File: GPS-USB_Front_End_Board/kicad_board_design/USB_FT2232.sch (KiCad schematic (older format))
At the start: 38 parts, among them J1 Micro-USB Connector, U1 93LCxxB, U2 FT2232HL-REEL, U3 L4931 LDO, Y1 12MHz Crystal

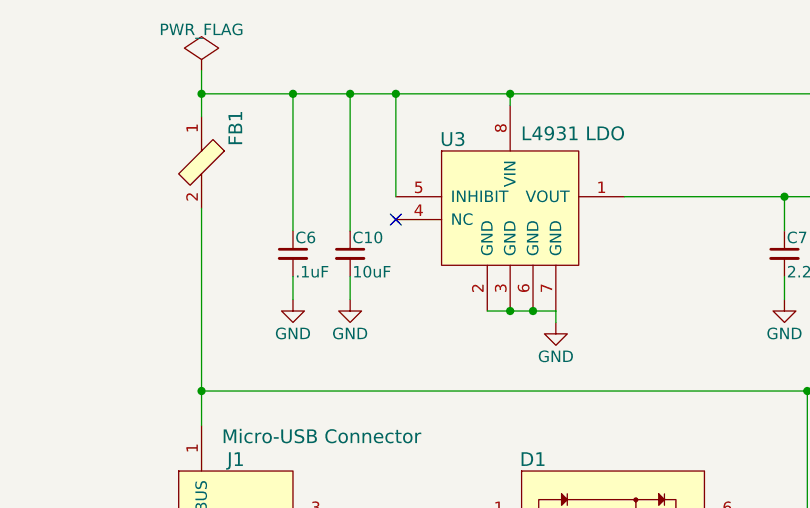
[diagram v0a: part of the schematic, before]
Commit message: Fix 3.3V LDO inhibit polarity.
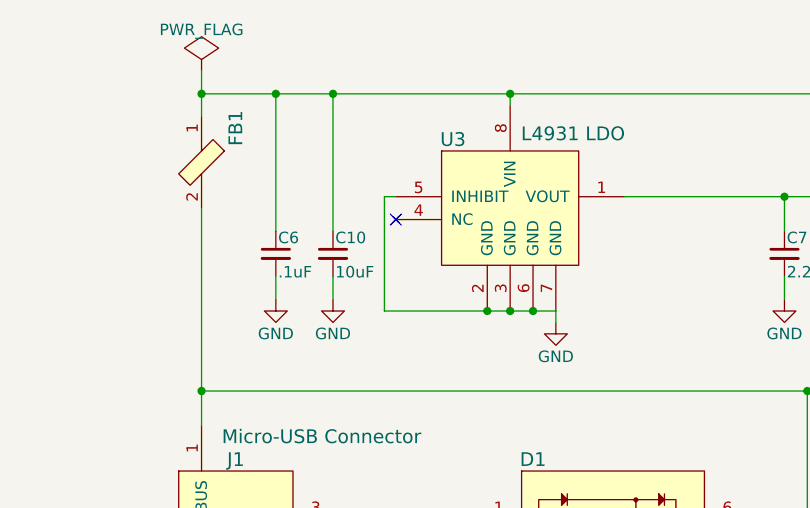
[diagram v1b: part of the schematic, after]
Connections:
- net +5V: no longer U3.5 (INHIBIT)
- net GND: now also U3.5 (INHIBIT)
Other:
- moved on the sheet: C10, C6

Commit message: Change out micro-usb connector to one with thru holes.
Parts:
- J1: footprint digikey-footprints:USB_Micro_B_Female_10118192 -> digikey-footprints:USB_Micro_B_Female_10118194-0001LF; Digi-Key_PN 609-4613-1-ND -> 609-4618-6-ND; MPN 10118192-0001LF -> 10118194-0001LF
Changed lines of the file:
@@
 F 0 "J1" H 7450 3000 60  0000 C CNN
 F 1 "Micro-USB Connector" H 7825 3100 60  0000 C CNN
-F 2 "digikey-footprints:USB_Micro_B_Female_10118192" H 7600 2950 60  0001 L CNN
+F 2 "digikey-footprints:USB_Micro_B_Female_10118194-0001LF" H 7600 2950 60  0001 L CNN
 F 3 "https://cdn.amphenol-icc.com/media/wysiwyg/files/drawing/10118192.pdf" H 7600 3050 60  0001 L CNN
-F 4 "609-4613-1-ND" H 7600 3150 60  0001 L CNN "Digi-Key_PN"
-F 5 "10118192-0001LF" H 7600 3250 60  0001 L CNN "MPN"
+F 4 "609-4618-6-ND" H 7600 3150 60  0001 L CNN "Digi-Key_PN"
+F 5 "10118194-0001LF" H 7600 3250 60  0001 L CNN "MPN"
 F 6 "Connectors, Interconnects" H 7600 3350 60  0001 L CNN "Category"
 F 7 "USB, DVI, HDMI Connectors" H 7600 3450 60  0001 L CNN "Family"

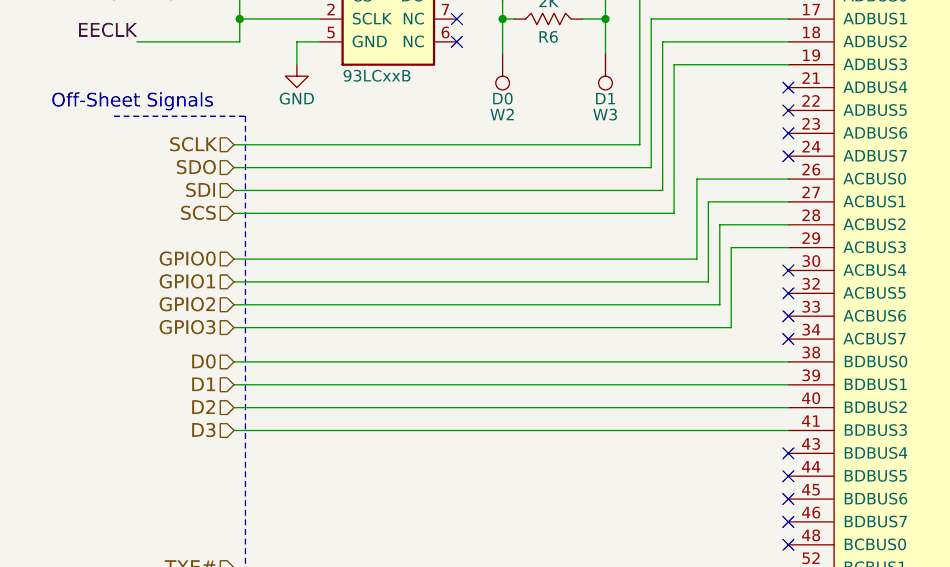
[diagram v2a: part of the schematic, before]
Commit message: Update to MAX2771.  Changes to decoupling caps, Remove ANTFLAG, IDLE signals.  Add explicit antenna bias.  New matching network for LNA input.  Remove bypass for SAW filter.
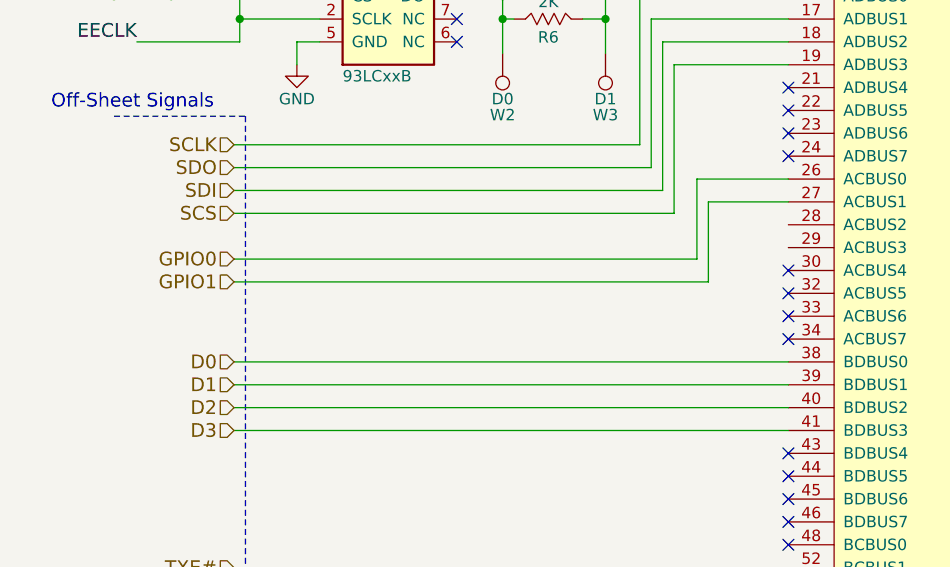
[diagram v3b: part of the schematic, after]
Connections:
- net GPIO2: no longer names the net of U2.28 (ACBUS2)
- net GPIO3: no longer names the net of U2.29 (ACBUS3)
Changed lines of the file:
@@
 Text HLabel 1425 4850 0    60   Input ~ 0
 SDI
-Text HLabel 1425 5150 0    60   Input ~ 0
-GPIO0
 Text HLabel 1425 5250 0    60   Input ~ 0
 GPIO1
-Text HLabel 1425 5350 0    60   Input ~ 0
-GPIO2
-Text HLabel 1425 5450 0    60   Input ~ 0
-GPIO3
 Text Label 8450 6150 2    60   ~ 0
 RESETIN#
@@
 	3450 4800 3450 5150
 Wire Wire Line
-	3450 5150 1425 5150
-Wire Wire Line
 	3850 4900 3500 4900
 Wire Wire Line
@@
 Wire Wire Line
 	3500 5250 1425 5250
-Wire Wire Line
-	3850 5000 3550 5000
-Wire Wire Line
-	3550 5000 3550 5350
-Wire Wire Line
-	3550 5350 1425 5350
-Wire Wire Line
-	3850 5100 3600 5100
-Wire Wire Line
-	3600 5100 3600 5450
-Wire Wire Line
-	3600 5450 1425 5450
 Wire Wire Line
 	2600 4100 2650 4100
@@
 Wire Wire Line
 	8100 1350 8100 1850
+Wire Wire Line
+	3450 5150 1425 5150
+Text HLabel 1425 5150 0    60   Input ~ 0
+GPIO0
 $EndSCHEMATC

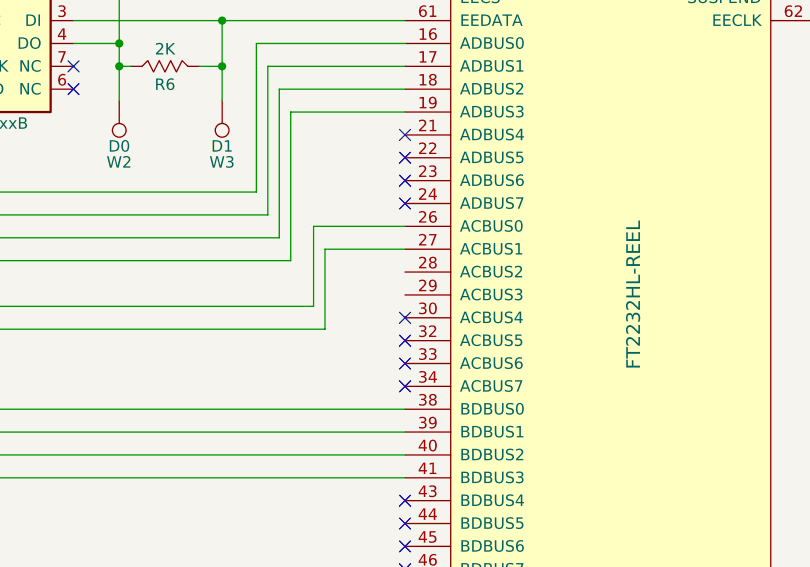
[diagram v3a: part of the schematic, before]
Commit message: Add some footprints, annotate new parts, generate netlist, EDR check.
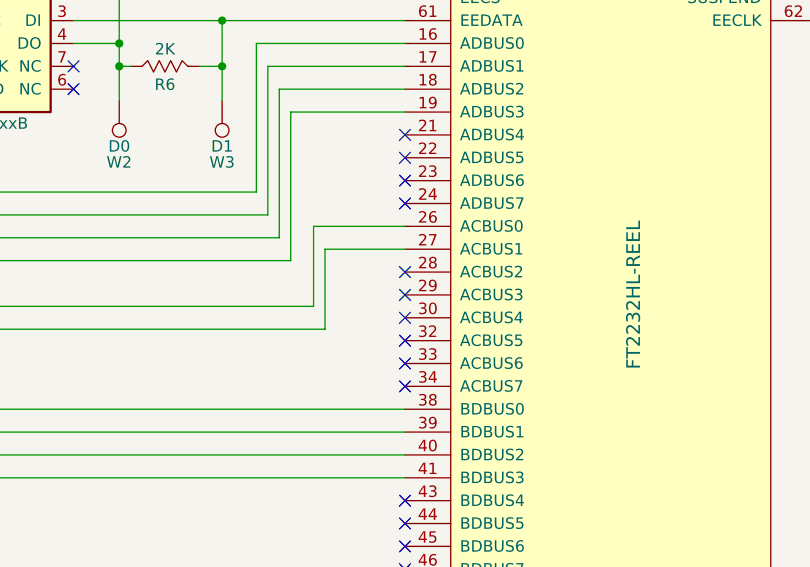
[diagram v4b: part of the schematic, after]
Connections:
- no-connect marks 22 -> 24
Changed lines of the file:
@@
 Text HLabel 1425 5150 0    60   Input ~ 0
 GPIO0
+NoConn ~ 3850 5100
+NoConn ~ 3850 5000
 $EndSCHEMATC

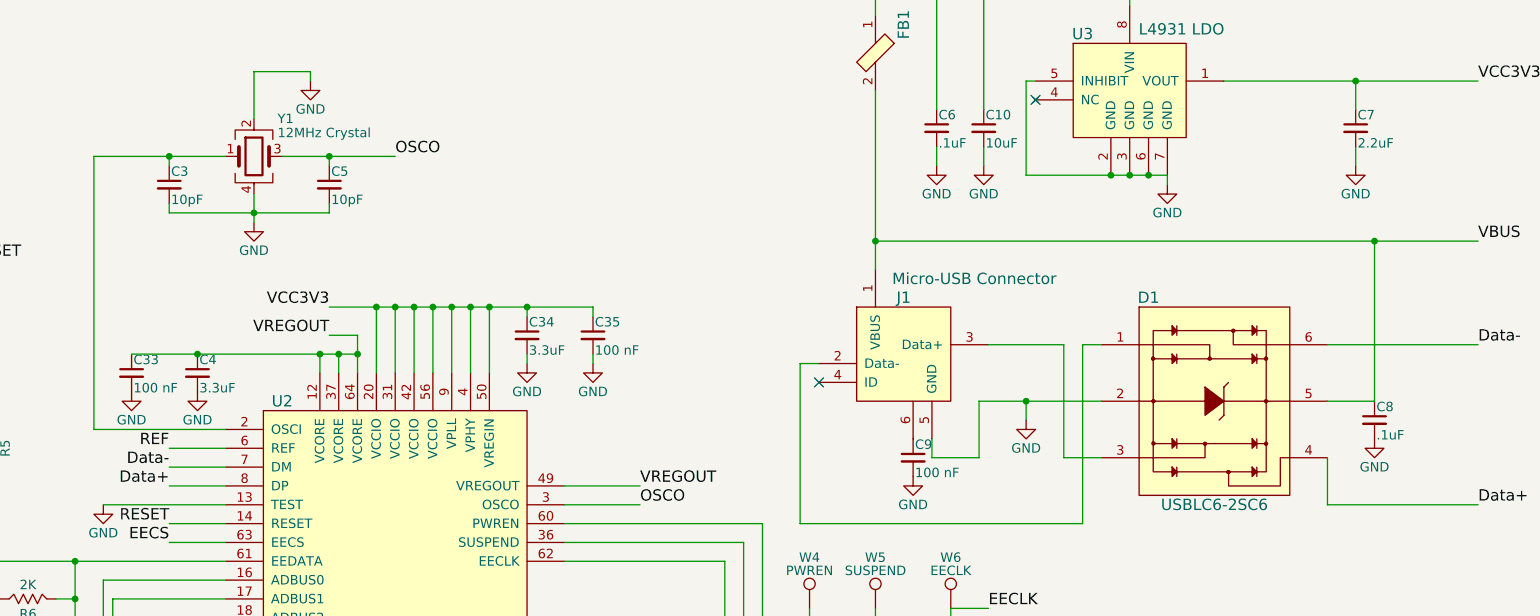
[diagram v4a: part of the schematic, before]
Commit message: Fix value display on EEPROM.  Consolidate some part values.
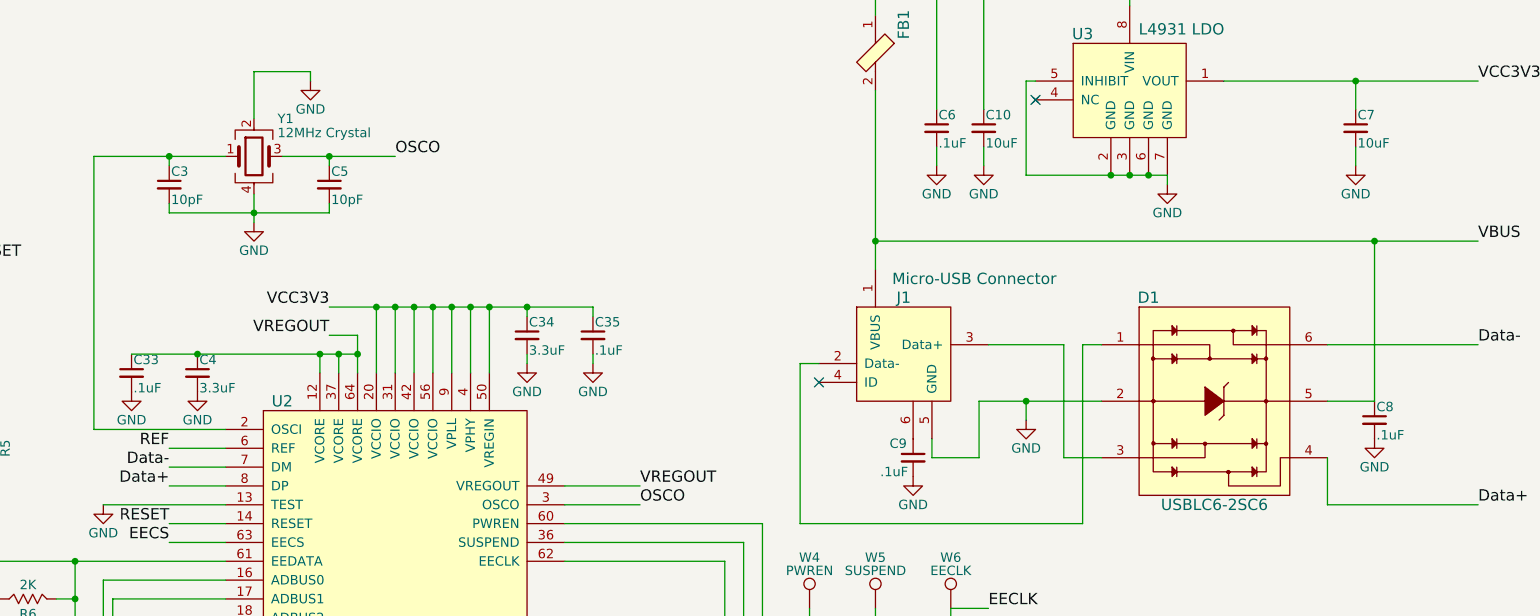
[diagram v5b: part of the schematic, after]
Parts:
- C33, C35, C9: value 100 nF -> .1uF
- C7: value 2.2uF -> 10uF; footprint Capacitors_SMD:C_0805_HandSoldering -> Capacitors_SMD:C_0805; MFR TDK -> Samsung; MPN C2012X7R1C225K125AB -> CL21A106KPFNNNG; SPN 445-1420-1-ND -> 1276-6456-1-ND
- D1: SPN 497-5235-1-ND USB -> 497-5235-1-ND
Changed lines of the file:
@@
 F 13 "STMicro" H 0   0   50  0001 C CNN "MFR"
 F 14 "Digikey" H 0   0   50  0001 C CNN "SPR"
-F 15 "497-5235-1-ND USB" H 0   0   50  0001 C CNN "SPN"
+F 15 "497-5235-1-ND" H 0   0   50  0001 C CNN "SPN"
 F 16 "-" H 0   0   50  0001 C CNN "SPURL"
 	1    9100 3050
@@
 $EndComp
 $Comp
-L C_Small C33
-U 1 1 5B46ED5F
-P 3350 2900
-F 0 "C33" H 3360 2970 50  0000 L CNN
-F 1 "100 nF" H 3360 2820 50  0000 L CNN
-F 2 "Capacitors_SMD:C_0402" H 3350 2900 50  0001 C CNN
-F 3 "" H 3350 2900 50  0001 C CNN
-F 4 "TDK" H 0   0   50  0001 C CNN "MFR"
-F 5 "CGA2B1X7R1C104K050BC" H 0   0   50  0001 C CNN "MPN"
-F 6 "Digikey" H 0   0   50  0001 C CNN "SPR"
-F 7 "445-5613-1-ND" H 0   0   50  0001 C CNN "SPN"
-F 8 "-" H 0   0   50  0001 C CNN "SPURL"
-	1    3350 2900
-	1    0    0    -1
-$EndComp
-$Comp
 L GND #PWR018
 U 1 1 5B46F0D4
@@
 $EndComp
 $Comp
-L C_Small C35
-U 1 1 5B46F3B3
-P 5800 2700
-F 0 "C35" H 5810 2770 50  0000 L CNN
-F 1 "100 nF" H 5810 2620 50  0000 L CNN
-F 2 "Capacitors_SMD:C_0402" H 5800 2700 50  0001 C CNN
-F 3 "" H 5800 2700 50  0001 C CNN
-F 4 "TDK" H 0   0   50  0001 C CNN "MFR"
-F 5 "CGA2B1X7R1C104K050BC" H 0   0   50  0001 C CNN "MPN"
-F 6 "Digikey" H 0   0   50  0001 C CNN "SPR"
-F 7 "445-5613-1-ND" H 0   0   50  0001 C CNN "SPN"
-F 8 "-" H 0   0   50  0001 C CNN "SPURL"
-	1    5800 2700
-	1    0    0    -1
-$EndComp
-$Comp
 L GND #PWR019
 U 1 1 5B46F495
@@
 F 3 "" H 5800 2850 50  0000 C CNN
 	1    5800 2850
-	1    0    0    -1
-$EndComp
-$Comp
-L C_Small C9
-U 1 1 5B5D53D2
-P 7500 3350
-F 0 "C9" H 7510 3420 50  0000 L CNN
-F 1 "100 nF" H 7510 3270 50  0000 L CNN
-F 2 "Capacitors_SMD:C_0402" H 7500 3350 50  0001 C CNN
-F 3 "" H 7500 3350 50  0001 C CNN
-F 4 "TDK" H 0   0   50  0001 C CNN "MFR"
-F 5 "CGA2B1X7R1C104K050BC" H 0   0   50  0001 C CNN "MPN"
-F 6 "Digikey" H 0   0   50  0001 C CNN "SPR"
-F 7 "445-5613-1-ND" H 0   0   50  0001 C CNN "SPN"
-F 8 "-" H 0   0   50  0001 C CNN "SPURL"
-	1    7500 3350
 	1    0    0    -1
 $EndComp
@@
 	1    3050 4250
 	1    0    0    1
-$EndComp
-$Comp
-L C_Small C7
-U 1 1 5B5B2330
-P 9850 1600
-F 0 "C7" H 9860 1670 50  0000 L CNN
-F 1 "2.2uF" H 9860 1520 50  0000 L CNN
-F 2 "Capacitors_SMD:C_0805_HandSoldering" H 9850 1600 50  0001 C CNN
-F 3 "" H 9850 1600 50  0001 C CNN
-F 4 "TDK" H 0   0   50  0001 C CNN "MFR"
-F 5 "C2012X7R1C225K125AB" H 0   0   50  0001 C CNN "MPN"
-F 6 "Digikey" H 0   0   50  0001 C CNN "SPR"
-F 7 "445-1420-1-ND" H 0   0   50  0001 C CNN "SPN"
-F 8 "-" H 0   0   50  0001 C CNN "SPURL"
-	1    9850 1600
-	1    0    0    -1
 $EndComp
 Text Label 10450 900  0    60   ~ 0
@@
 NoConn ~ 3850 5100
 NoConn ~ 3850 5000
+$Comp
+L C_Small C7
+U 1 1 5D400776
+P 9850 1600
+F 0 "C7" H 9860 1670 50  0000 L CNN
+F 1 "10uF" H 9860 1520 50  0000 L CNN
+F 2 "Capacitors_SMD:C_0805" H 9850 1600 50  0001 C CNN
+F 3 "" H 9850 1600 50  0001 C CNN
+F 4 "Samsung" H -625 -3350 50  0001 C CNN "MFR"
+F 5 "CL21A106KPFNNNG" H -625 -3350 50  0001 C CNN "MPN"
+F 6 "Digikey" H -625 -3350 50  0001 C CNN "SPR"
+F 7 "1276-6456-1-ND" H -625 -3350 50  0001 C CNN "SPN"
+F 8 "-" H -625 -3350 50  0001 C CNN "SPURL"
+	1    9850 1600
+	1    0    0    -1
+$EndComp
+$Comp
+L C_Small C35
+U 1 1 5D449A5A
+P 5800 2700
+F 0 "C35" H 5810 2770 50  0000 L CNN
+F 1 ".1uF" H 5810 2620 50  0000 L CNN
+F 2 "Capacitors_SMD:C_0402" H 5800 2700 50  0001 C CNN
+F 3 "" H 5800 2700 50  0001 C CNN
+F 4 "TDK" H -1900 1100 50  0001 C CNN "MFR"
+F 5 "CGA2B1X7R1C104K050BC" H -1900 1100 50  0001 C CNN "MPN"
+F 6 "Digikey" H -1900 1100 50  0001 C CNN "SPR"
+F 7 "445-5613-1-ND" H -1900 1100 50  0001 C CNN "SPN"
+F 8 "-" H -1900 1100 50  0001 C CNN "SPURL"
+	1    5800 2700
+	1    0    0    -1
+$EndComp
+$Comp
+L C_Small C33
+U 1 1 5D449E66
+P 3350 2900
+F 0 "C33" H 3360 2970 50  0000 L CNN
+F 1 ".1uF" H 3360 2820 50  0000 L CNN
+F 2 "Capacitors_SMD:C_0402" H 3350 2900 50  0001 C CNN
+F 3 "" H 3350 2900 50  0001 C CNN
+F 4 "TDK" H -4350 1300 50  0001 C CNN "MFR"
+F 5 "CGA2B1X7R1C104K050BC" H -4350 1300 50  0001 C CNN "MPN"
+F 6 "Digikey" H -4350 1300 50  0001 C CNN "SPR"
+F 7 "445-5613-1-ND" H -4350 1300 50  0001 C CNN "SPN"
+F 8 "-" H -4350 1300 50  0001 C CNN "SPURL"
+	1    3350 2900
+	1    0    0    -1
+$EndComp
+$Comp
+L C_Small C9
+U 1 1 5D44A34B
+P 7500 3350
+F 0 "C9" H 7375 3425 50  0000 L CNN
+F 1 ".1uF" H 7325 3275 50  0000 L CNN
+F 2 "Capacitors_SMD:C_0402" H 7500 3350 50  0001 C CNN
+F 3 "" H 7500 3350 50  0001 C CNN
+F 4 "TDK" H -200 1750 50  0001 C CNN "MFR"
+F 5 "CGA2B1X7R1C104K050BC" H -200 1750 50  0001 C CNN "MPN"
+F 6 "Digikey" H -200 1750 50  0001 C CNN "SPR"
+F 7 "445-5613-1-ND" H -200 1750 50  0001 C CNN "SPN"
+F 8 "-" H -200 1750 50  0001 C CNN "SPURL"
+	1    7500 3350
+	1    0    0    -1
+$EndComp
 $EndSCHEMATC
